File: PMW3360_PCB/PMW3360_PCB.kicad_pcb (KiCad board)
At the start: 2 copper layers, 27 x 28 mm, 20 parts, among them J1 Conn_01x08, U1 PMW3360DM-T2QU, U2 TPS73601DBV

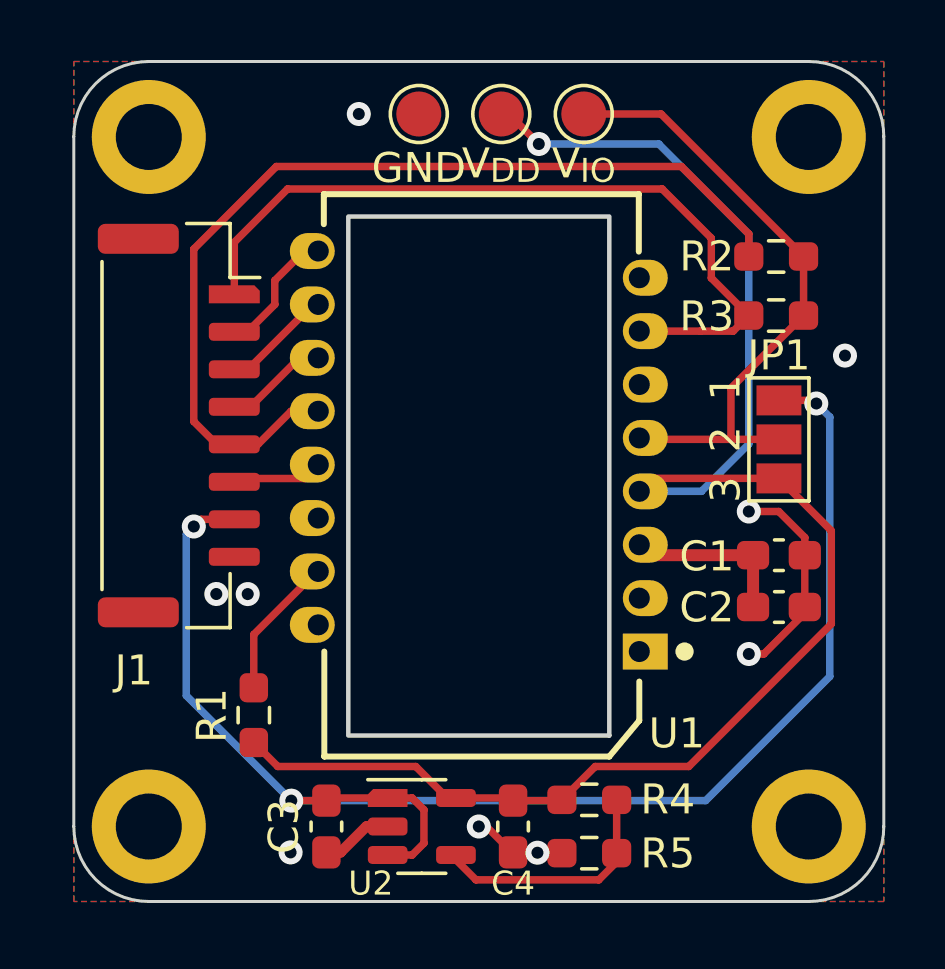
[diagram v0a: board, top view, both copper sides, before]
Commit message: Replace JST GH 1.25 connector with 0.5mm FPC
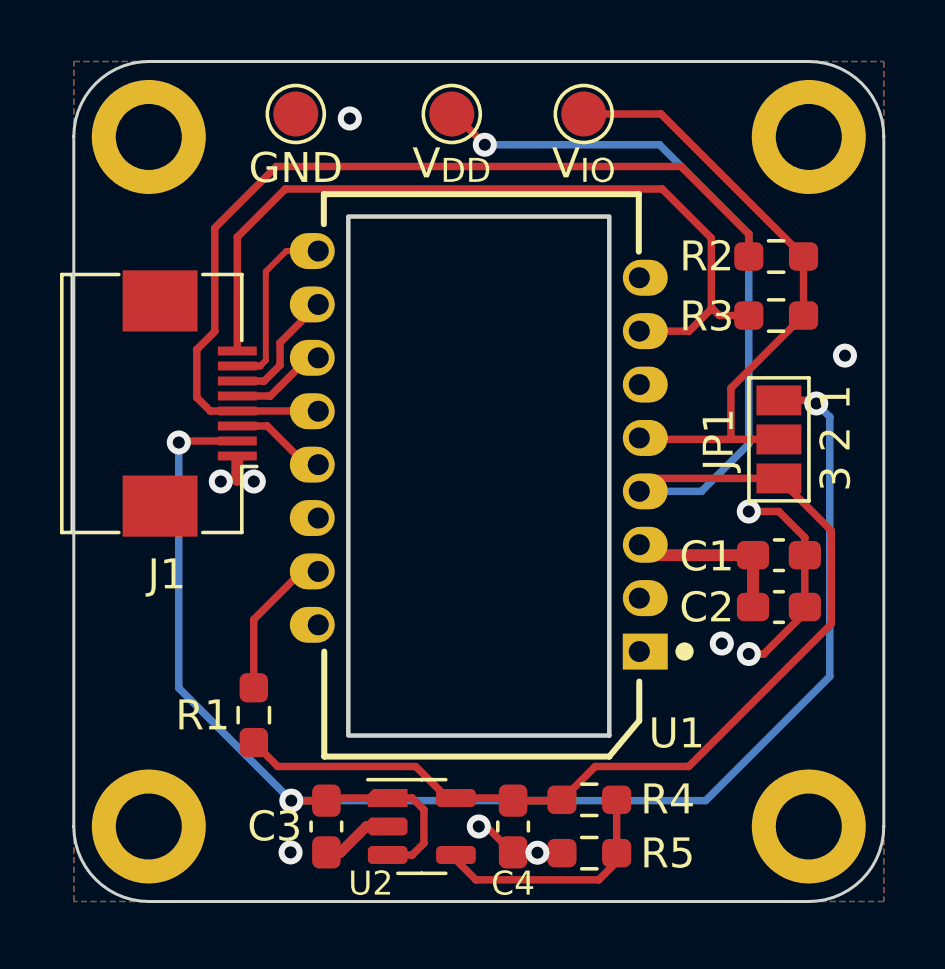
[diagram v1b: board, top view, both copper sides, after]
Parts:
- J1: footprint Connector_JST:JST_GH_SM08B-GHS-TB_1x08-1MP_P1.25mm_Horizontal -> ErgoSNM_Keyboard:FPC_8P_0.5mm_AFC01-S08FCA-00
- moved TP3 4.10 mm to (181.0, 116.3)
- moved TP2 1.65 mm to (186.2, 116.3)
- moved J1 1.28 mm to (176.1, 125.9), turned to 90 degrees
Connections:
- J1 pad 1: /RESET -> GND
- J1 pad 2: /MOTION -> V_IN
- J1 pad 3: /SCLK -> /CS
- J1 pad 4: /MOSI -> /MISO
- J1 pad 5: /MISO -> /MOSI
- J1 pad 6: /CS -> /SCLK
- J1 pad 7: V_IN -> /MOTION
- J1 pad 8: GND -> /RESET
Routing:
- net V_IN: track 50.2 -> 52.8 mm
- net /MOTION: track 4.38 -> 6.49 mm
- net VDD: track 54.1 -> 55.8 mm
- net /MISO: track 32.0 -> 30.5 mm
- net /RESET: track 26.0 -> 27.4 mm
- net /CS: track 3.04 -> 3.89 mm
- net /SCLK: track 3.70 -> 4.37 mm
- net GND: track 12.7 -> 13.4 mm, vias 9 -> 10

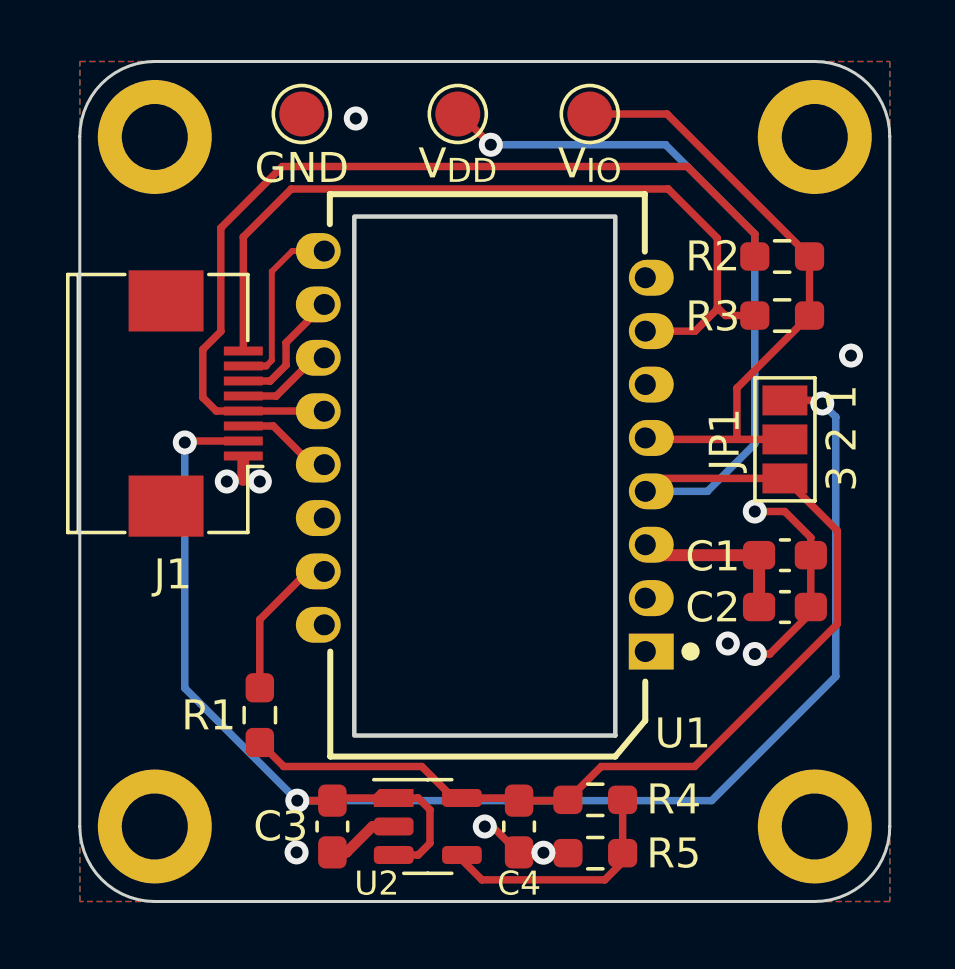
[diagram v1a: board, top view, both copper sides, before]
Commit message: Reduce board size
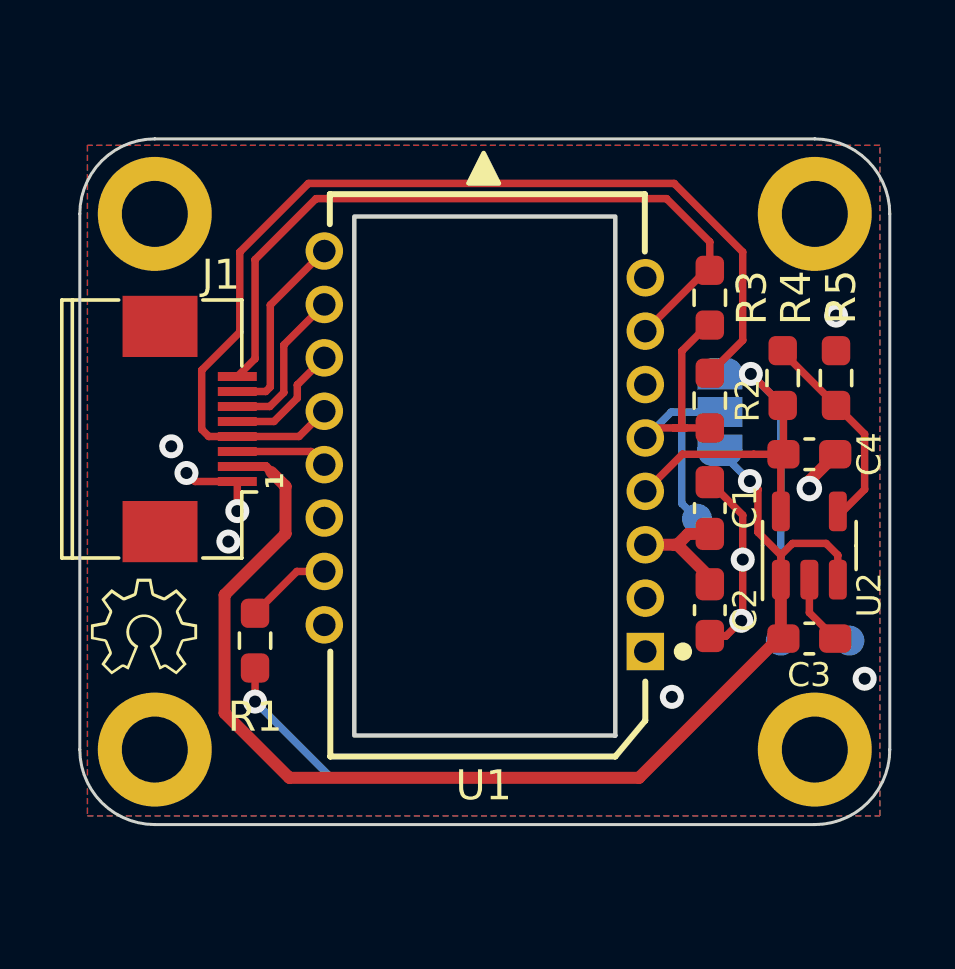
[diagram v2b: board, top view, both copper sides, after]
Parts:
- J1: footprint ErgoSNM_Keyboard:FPC_8P_0.5mm_AFC01-S08FCA-00 -> PMW3360_PCB:FPC_8P_0.5mm_AFC01-S08FCA-00
- JP1: footprint Jumper:SolderJumper-3_P1.3mm_Open_Pad1.0x1.5mm_NumberLabels -> Jumper:SolderJumper-3_P1.3mm_Open_RoundedPad1.0x1.5mm_NumberLabels; moved to B.Cu
- R3: value DNI -> 10k
- R4: value Adj_R1 -> 28k
- R5: value Adj_R2 -> 56.2k
- TP1: value VIO TestPoint -> V_{IO} Test; footprint TestPoint:TestPoint_Pad_D1.5mm -> TestPoint:TestPoint_Pad_D1.0mm; moved to B.Cu
- TP2: value VDD TestPoint -> V_{DD} Test; footprint TestPoint:TestPoint_Pad_D1.5mm -> TestPoint:TestPoint_Pad_D1.0mm; moved to B.Cu
- TP3: value GND TestPoint -> GND Test; footprint TestPoint:TestPoint_Pad_D1.5mm -> TestPoint:TestPoint_Pad_D1.0mm; moved to B.Cu
- moved TP3 25.3 mm to (199.3, 133.8), turned to 180 degrees
- moved TP2 20.6 mm to (197.0, 133.8), turned to 180 degrees
- moved R5 17.8 mm to (198.8, 125.1), turned to 90 degrees
- moved C3 17.1 mm to (198.0, 133.8), turned to 0 degrees
- moved U2 15.8 mm to (198.0, 130.7), turned to 90 degrees
- moved C4 15.7 mm to (198.0, 127.6), turned to 0 degrees
- moved R4 15.4 mm to (197.1, 125.1), turned to 90 degrees
- moved TP1 14.0 mm to (194.2, 129.8), turned to 180 degrees
- moved R2 5.37 mm to (194.6, 125.8), turned to 90 degrees
- moved C1 2.96 mm to (194.6, 129.4), turned to 90 degrees
- moved H1 2.56 mm to (176.1, 137.5)
- moved H2 2.56 mm to (198.1, 137.5)
- moved H3 2.56 mm to (198.1, 119.6)
- moved H4 2.56 mm to (176.1, 119.6)
- moved C2 2.51 mm to (194.6, 132.8), turned to -90 degrees
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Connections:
- net V_IN renamed V_{IN}
- net V_IO renamed V_{IO}
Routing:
- net VDD: track 55.8 -> 42.1 mm, vias 1 -> 2
- net V_{IN}: track 52.8 -> 41.9 mm, vias 3 -> 1
- net V_{IO}: track 21.1 -> 13.0 mm
- net /MISO: track 30.5 -> 34.1 mm
- net /RESET: track 27.4 -> 24.7 mm
- net Net-(U1-LED_P): track 5.09 -> 2.89 mm
- net Net-(U1-VDDPIX): track 5.77 -> 4.06 mm
- net Net-(U2-FB): track 8.11 -> 6.95 mm
- net /SCLK: track 4.37 -> 5.24 mm
- net /CS: track 3.89 -> 3.08 mm
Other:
- board size 27 x 28 mm -> 27 x 22.9 mm
- board text added: "${TITLE} v${REVISION}"
- board text added: "1"
- board text added: "JP1: [1-2 3] V_{IO}=V_{IN} [1 2-3] V_{IO}=V_{DD}"
- board text added: "~{Reset}"
- board text removed: "${TITLE} Rev ${REVISION}"
- board text removed: "JP1: [1-2 3]V_{IO}=V_{IN} [1 2-3]V_{IO}=V_{DD}"
- board text removed: "~{RST}"

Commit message: Update schematic
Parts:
- J1: value Conn_01x08 -> Interface
- TP1: value V_{IO} Test -> V_{IO}
- TP2: value V_{DD} Test -> V_{DD}
- TP3: value GND Test -> GND
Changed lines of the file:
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@@
     (title "PMW3360 PCB")
     (rev "3.2")
+    (company "SideraKB")
     (comment 1 "PMW3360DM-T2QU optical mouse sensor breakout board")
     (comment 2 "MIT License (Open Source Hardware)")
@@
         (effects (font (size 1 1) (thickness 0.15)))
     )
-    (fp_text value "Conn_01x08" (at 0 0.5 90 unlocked) (layer "F.Fab")
+    (fp_text value "Interface" (at 0 0.5 90 unlocked) (layer "F.Fab")
         (effects (font (size 1 1) (thickness 0.15)))
     )
@@
         (effects (font (size 1 1) (thickness 0.15)) (justify mirror))
     )
-    (fp_text value "V_{DD} Test" (at 0 -1.55) (layer "B.Fab")
+    (fp_text value "V_{DD}" (at 0 -1.55) (layer "B.Fab")
         (effects (font (size 1 1) (thickness 0.15)) (justify mirror))
     )
@@
         (effects (font (size 1 1) (thickness 0.15)) (justify mirror))
     )
-    (fp_text value "V_{IO} Test" (at 0 -1.55) (layer "B.Fab")
+    (fp_text value "V_{IO}" (at 0 -1.55) (layer "B.Fab")
         (effects (font (size 1 1) (thickness 0.15)) (justify mirror))
     )
@@
         (effects (font (size 1 1) (thickness 0.15)) (justify mirror))
     )
-    (fp_text value "GND Test" (at 0 -1.55) (layer "B.Fab")
+    (fp_text value "GND" (at 0 -1.55) (layer "B.Fab")
         (effects (font (size 1 1) (thickness 0.15)) (justify mirror))
     )
@@
   (segment (start 193.557 130.6418) (end 193.917 130.2818) (width 0.4) (layer "F.Cu") (net 1))
   (segment (start 193.917 130.2818) (end 194.639 130.2818) (width 0.4) (layer "F.Cu") (net 1))
-  (segment (start 195.1793 133.6843) (end 194.639 133.6843) (width 0.25) (layer "F.Cu") (net 2))
+  (segment (start 195.737 133.1266) (end 195.1793 133.6843) (width 0.25) (layer "F.Cu") (net 2))
   (segment (start 197.957 128.7688) (end 197.957 128.5148) (width 0.4) (layer "F.Cu") (net 2))
   (segment (start 197.957 132.9063) (end 198.8195 133.7688) (width 0.25) (layer "F.Cu") (net 2))
-  (segment (start 195.737 133.1266) (end 195.1793 133.6843) (width 0.25) (layer "F.Cu") (net 2))
-  (segment (start 195.737 129.6548) (end 195.737 133.1266) (width 0.25) (layer "F.Cu") (net 2))
   (segment (start 177.479 128.5338) (end 177.195 128.2498) (width 0.25) (layer "F.Cu") (net 2))
   (segment (start 178.889 128.5338) (end 178.889 129.5198) (width 0.25) (layer "F.Cu") (net 2))
-  (segment (start 194.639 128.5568) (end 195.737 129.6548) (width 0.25) (layer "F.Cu") (net 2))
+  (segment (start 195.737 129.6548) (end 195.737 133.1266) (width 0.25) (layer "F.Cu") (net 2))
   (segment (start 198.8195 127.6523) (end 198.8195 127.6258) (width 0.25) (layer "F.Cu") (net 2))
   (segment (start 178.889 128.5338) (end 177.479 128.5338) (width 0.25) (layer "F.Cu") (net 2))
+  (segment (start 195.1793 133.6843) (end 194.639 133.6843) (width 0.25) (layer "F.Cu") (net 2))
   (segment (start 197.957 128.5148) (end 198.8195 127.6523) (width 0.4) (layer "F.Cu") (net 2))
+  (segment (start 194.639 128.5568) (end 195.737 129.6548) (width 0.25) (layer "F.Cu") (net 2))
   (segment (start 197.957 131.8058) (end 197.957 132.9063) (width 0.25) (layer "F.Cu") (net 2))
   (via (at 193.374106 135.71235) (size 0.8) (drill 0.4) (layers "F.Cu" "B.Cu") (free) (net 2))
@@
   (segment (start 197.068 124.1733) (end 197.068 124.2203) (width 0.25) (layer "F.Cu") (net 13))
   (zone (net 2) (net_name "GND") (layers "F&B.Cu") (hatch edge 0.508)
-    (connect_pads (clearance 0.508))
+    (connect_pads (clearance 0.5))
     (min_thickness 0.254) (filled_areas_thickness no)
     (fill yes (thermal_gap 0.508) (thermal_bridge_width 0.508))
     (polygon
       (pts
-        (xy 173.893 139.6798)
+        (xy 173.889 139.8238)
         (xy 200.309 139.6798)
         (xy 200.309 117.3278)

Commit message: Rerounted
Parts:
- moved H1 53.2 mm to (137.6, 100.8)
- moved H2 53.2 mm to (159.6, 100.8)
- moved U1 53.0 mm to (148.6, 91.6)
- moved H3 52.9 mm to (159.6, 83.3)
- moved H4 52.9 mm to (137.6, 83.3)
- moved R4 52.8 mm to (158.8, 88.7)
- moved R5 52.8 mm to (160.5, 88.7)
- moved C1 52.8 mm to (156.3, 93.1)
- moved C2 52.8 mm to (156.3, 96.5)
- moved R2 52.8 mm to (156.3, 89.5)
- moved R3 52.8 mm to (156.3, 86.1)
- moved TP2 52.8 mm to (158.7, 97.5)
- moved TP3 52.8 mm to (161.0, 97.5)
- moved C3 52.8 mm to (159.6, 97.4)
- moved C4 52.8 mm to (159.6, 91.3)
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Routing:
- net GND: track 13.0 -> 107.2 mm, vias 10 -> 7
- net /MISO: track 34.1 -> 31.5 mm, vias 0 -> 1
- net Net-(U1-VDDPIX): track 4.06 -> 5.86 mm
- net /MOTION: track 6.44 -> 8.09 mm
- net VDD: track 42.1 -> 40.9 mm
- net V_{IN}: track 41.9 -> 41.4 mm
- net /RESET: track 24.7 -> 25.0 mm, vias 0 -> 2
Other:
- board size 27 x 22.9 mm -> 27 x 22.5 mm
- board text added: "2"
